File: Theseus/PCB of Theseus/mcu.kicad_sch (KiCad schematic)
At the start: 22 parts, among them J5 CN4 STDC14 (Programmer), U5 MX25L25645G, U6 STM32H750VBTx, Y1 ASE-4.000MHz-L-C-T

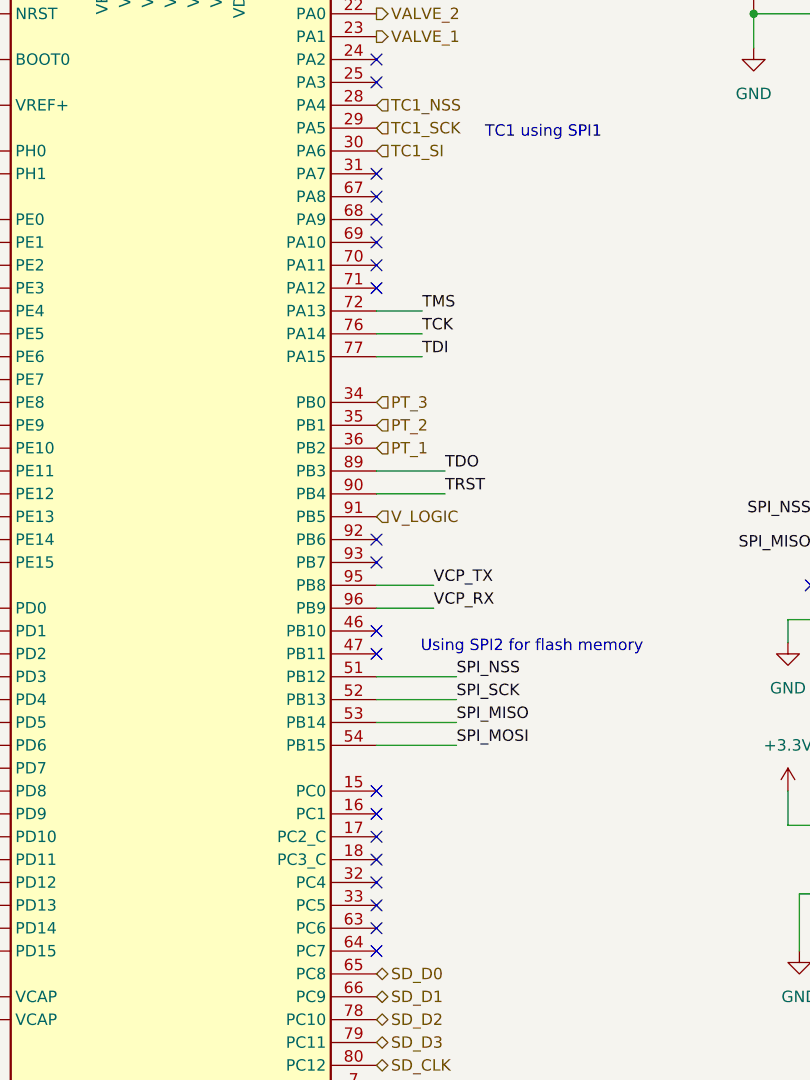
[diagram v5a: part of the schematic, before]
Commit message: Fix PT3 ADC
Updated PT3 to use valid ADC pin
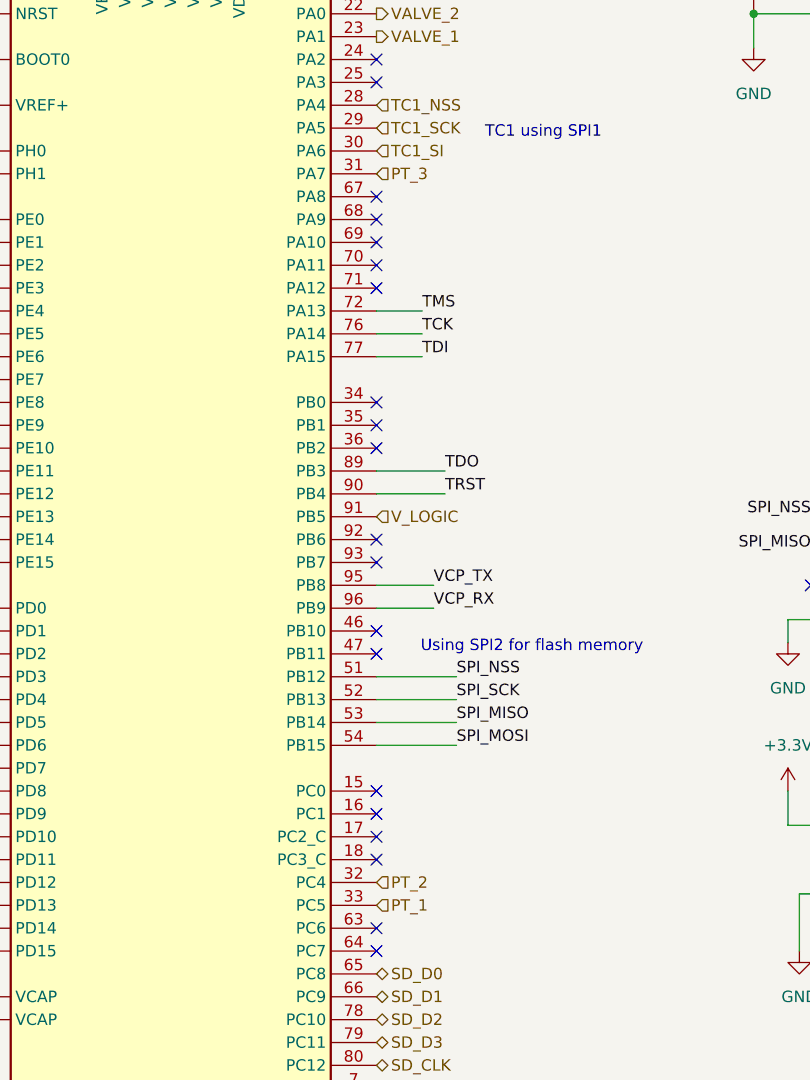
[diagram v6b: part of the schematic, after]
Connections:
- net PT_1: now also U6.33 (PC5); no longer U6.36 (PB2)
- net PT_2: now also U6.32 (PC4); no longer U6.35 (PB1)
- net PT_3: now also U6.31 (PA7); no longer U6.34 (PB0)
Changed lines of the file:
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@@
+	)
+	(no_connect
+		(at 115.57 86.36)
 	)
 	(no_connect
@@
 	)
 	(no_connect
+		(at 115.57 83.82)
+	)
+	(no_connect
 		(at 69.85 78.74)
 	)
@@
 	)
 	(no_connect
-		(at 115.57 55.88)
-	)
-	(no_connect
 		(at 163.83 101.6)
 	)
@@
 	)
 	(no_connect
-		(at 115.57 134.62)
-	)
-	(no_connect
 		(at 69.85 48.26)
 	)
@@
 	)
 	(no_connect
-		(at 115.57 137.16)
+		(at 115.57 81.28)
 	)
 	(no_connect
@@
 	(hierarchical_label "PT_1"
 		(shape input)
-		(at 115.57 86.36 0)
+		(at 115.57 137.16 0)
 		(effects
 			(font
@@
 	(hierarchical_label "PT_2"
 		(shape input)
-		(at 115.57 83.82 0)
+		(at 115.57 134.62 0)
 		(effects
 			(font
@@
 	(hierarchical_label "PT_3"
 		(shape input)
-		(at 115.57 81.28 0)
-		(effects
-			(font
+		(at 115.57 55.88 0)
+		(effects
+			(font

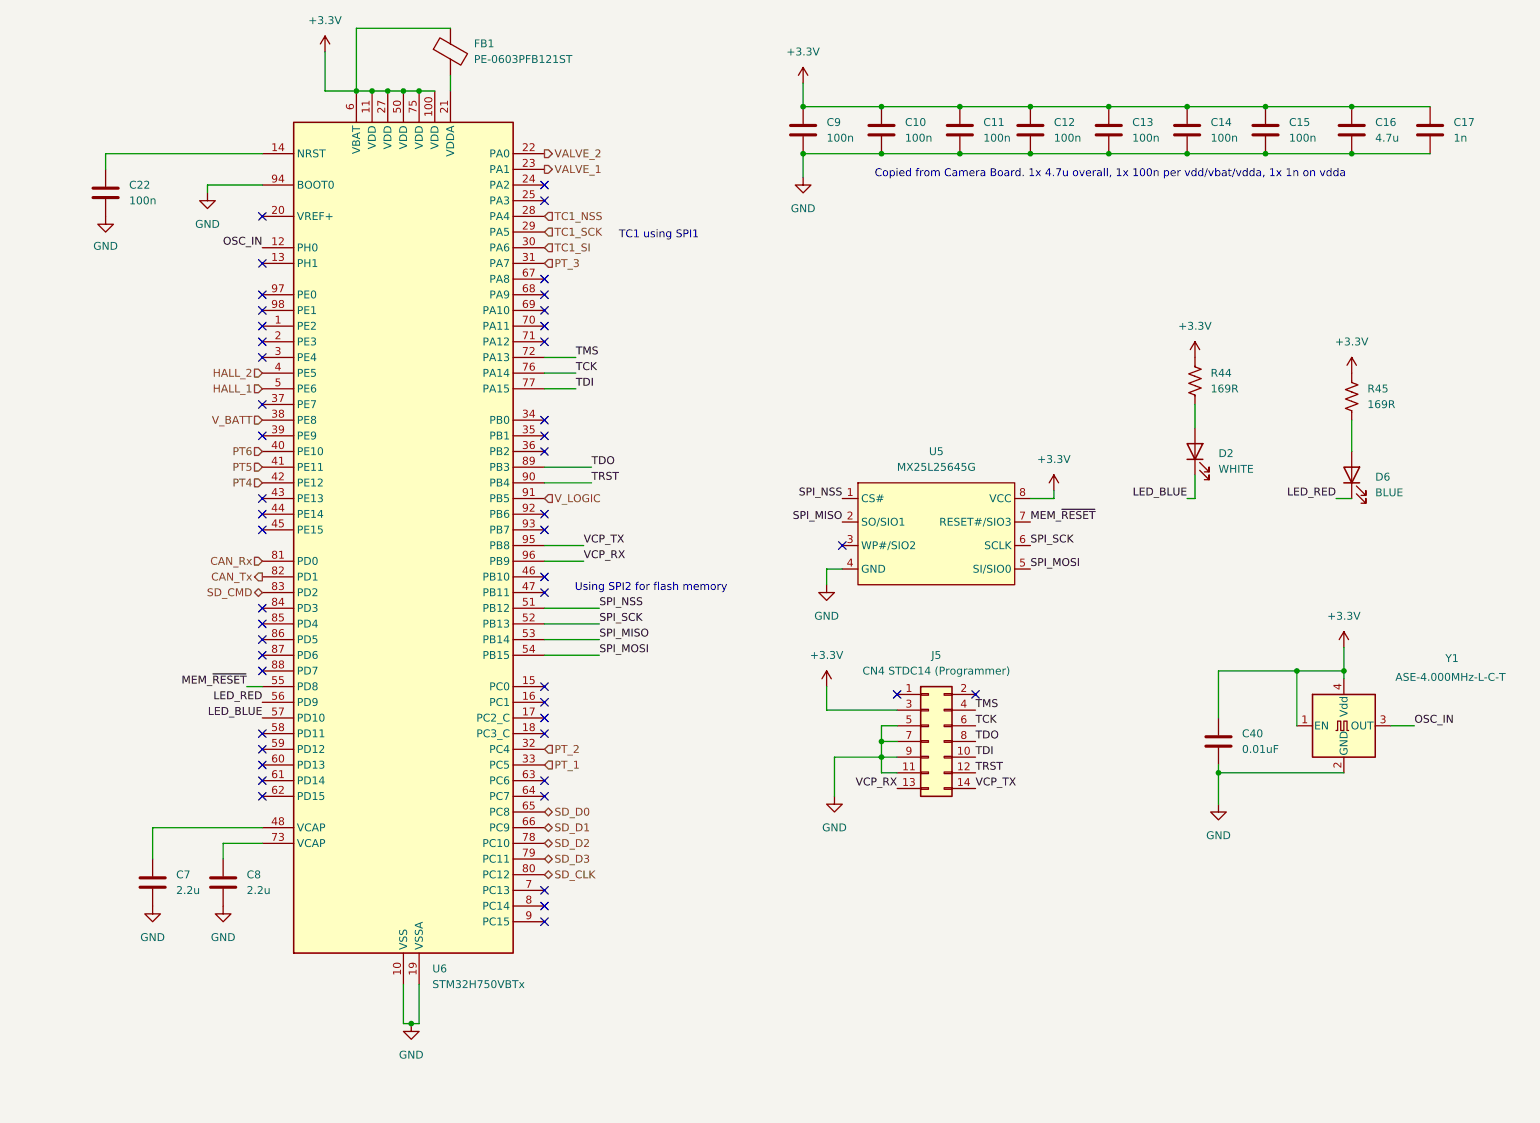
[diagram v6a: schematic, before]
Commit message: layout and routing + minor schematic changes
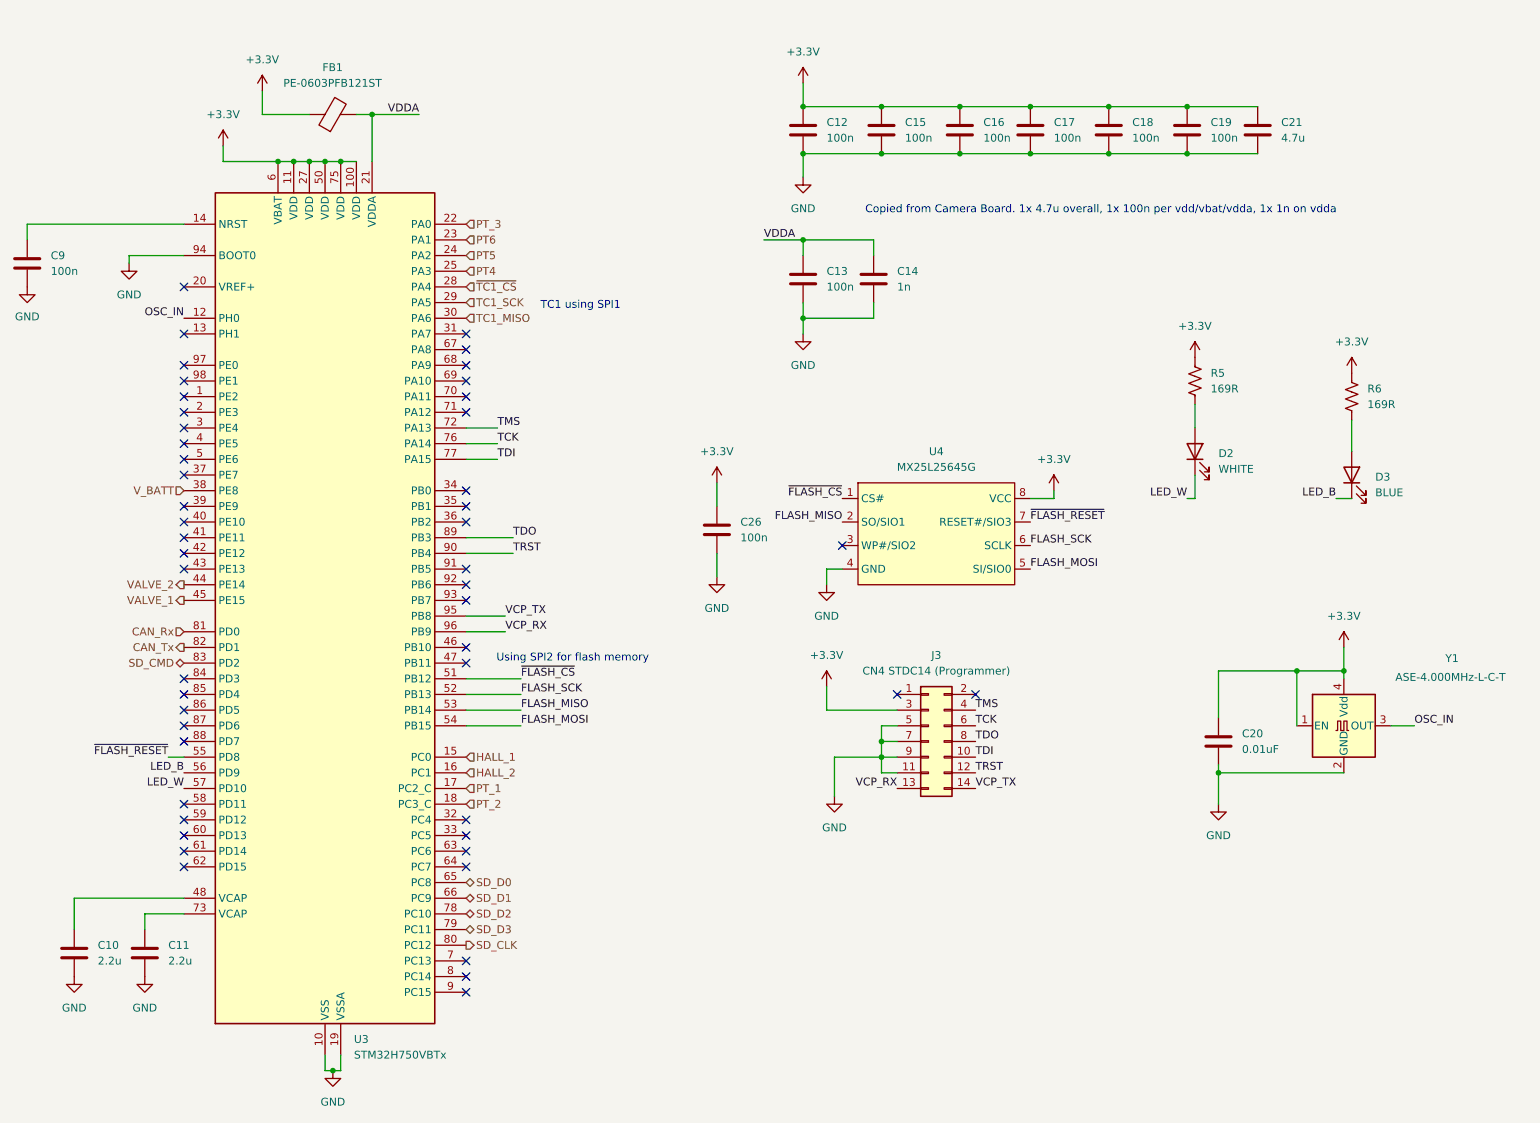
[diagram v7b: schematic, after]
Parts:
- added C26: 100n, Capacitor_SMD:C_0603_1608Metric_Pad1.08x0.95mm_HandSolder, symbol Device:C
- D2: footprint Diode_SMD:D_0603_1608Metric_Pad1.05x0.95mm_HandSolder -> LED_SMD:LED_1206_3216Metric_Pad1.42x1.75mm_HandSolder
- D3: renamed from D6; footprint Diode_SMD:D_0603_1608Metric_Pad1.05x0.95mm_HandSolder -> LED_SMD:LED_1206_3216Metric_Pad1.42x1.75mm_HandSolder
- renumbered C7 to C10, C8 to C11, C9 to C12, C15 to C13, C17 to C14, C10 to C15, C11 to C16, C12 to C17, C13 to C18, C14 to C19, C40 to C20, C16 to C21, C22 to C9, J5 to J3, R44 to R5, R45 to R6, U6 to U3, U5 to U4
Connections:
- net +3.3V: now also C26.1; no longer C13.1, C14.1
- net GND: now also C26.2
- net HALL_1: now also U3.15 (PC0); no longer U3.5 (PE6)
- net HALL_2: now also U3.16 (PC1); no longer U3.4 (PE5)
- net PT4: now also U3.25 (PA3); no longer U3.42 (PE12)
- net PT5: now also U3.24 (PA2); no longer U3.41 (PE11)
- net PT6: now also U3.23 (PA1); no longer U3.40 (PE10)
- net PT_1: now also U3.17 (PC2_C); no longer U3.33 (PC5)
- net PT_2: now also U3.18 (PC3_C); no longer U3.32 (PC4)
- net PT_3: now also U3.22 (PA0); no longer U3.31 (PA7)
- net VALVE_1: now also U3.45 (PE15); no longer U3.23 (PA1)
- net VALVE_2: now also U3.44 (PE14); no longer U3.22 (PA0)
- net VDDA: now reaches FB1.2, U3.21 (VDDA)
- net VDDA: now also C13.1, C14.1
- net LED_BLUE renamed LED_W
- net LED_RED renamed LED_B
- net MEM_~{RESET} renamed ~{FLASH_RESET}
- net SPI_MISO renamed FLASH_MISO
- net SPI_MOSI renamed FLASH_MOSI
- net SPI_NSS renamed ~{FLASH_CS}
- net SPI_SCK renamed FLASH_SCK
- net TC1_NSS renamed ~{TC1_CS}
- net TC1_SI renamed TC1_MISO
- net V_LOGIC: no longer names the net of U3.91 (PB5)
- no-connect marks 48 -> 49
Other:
- moved on the sheet: C10, C11, C13, C14, C21, C9, FB1, U3
